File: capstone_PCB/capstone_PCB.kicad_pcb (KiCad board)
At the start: 2 copper layers, 110 x 65 mm, 48 parts, among them J1 282837-4, J2 282837-4, J3 Barrel Jack, J4 282837-4, J5 Fan1, J6 Fan2, J7 12402012E212A, P1 282837-2, P3 282837-2, P4 282837-2, P5 282837-2, Q1 IRF4905PBF, U1 DEV-15583, U2 2472, U3 VNH5019ATR-E, U4 VNH5019ATR-E

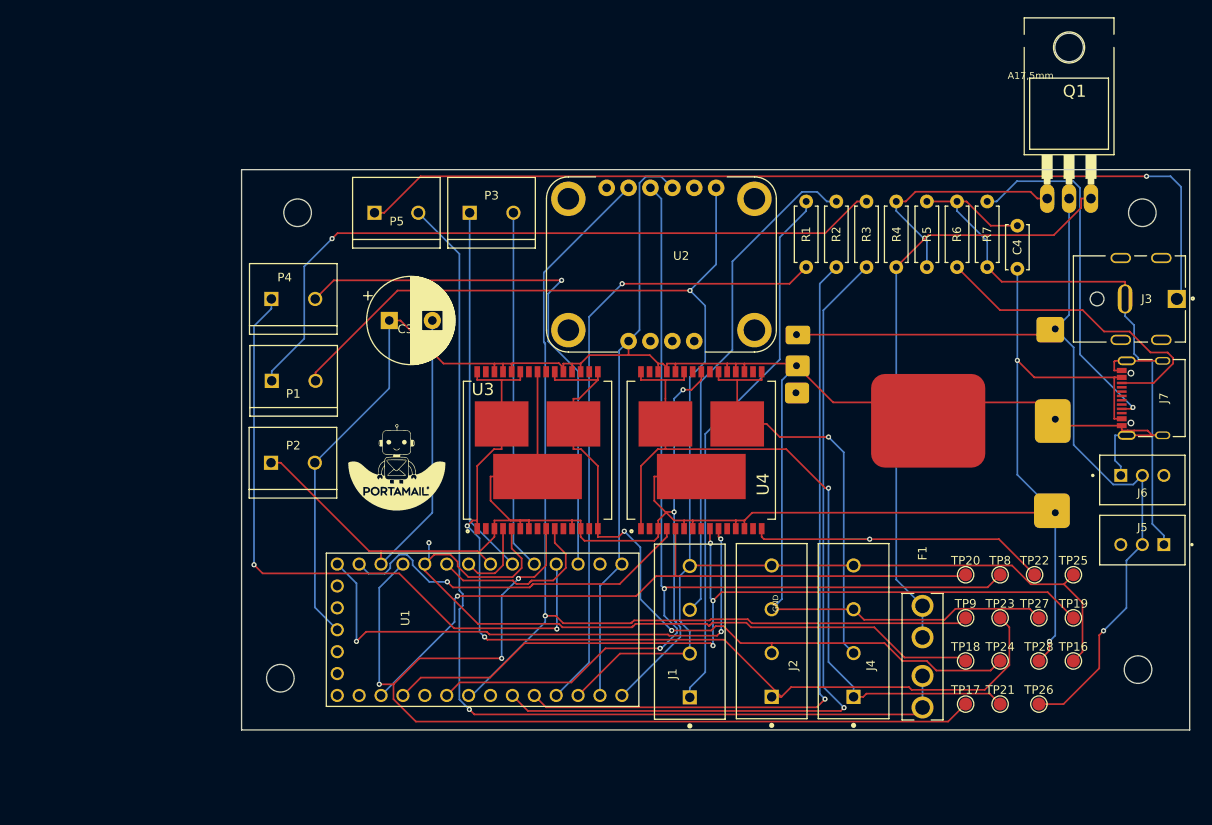
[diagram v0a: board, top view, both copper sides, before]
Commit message: Updated Capstone PCB to new iteration with esp32
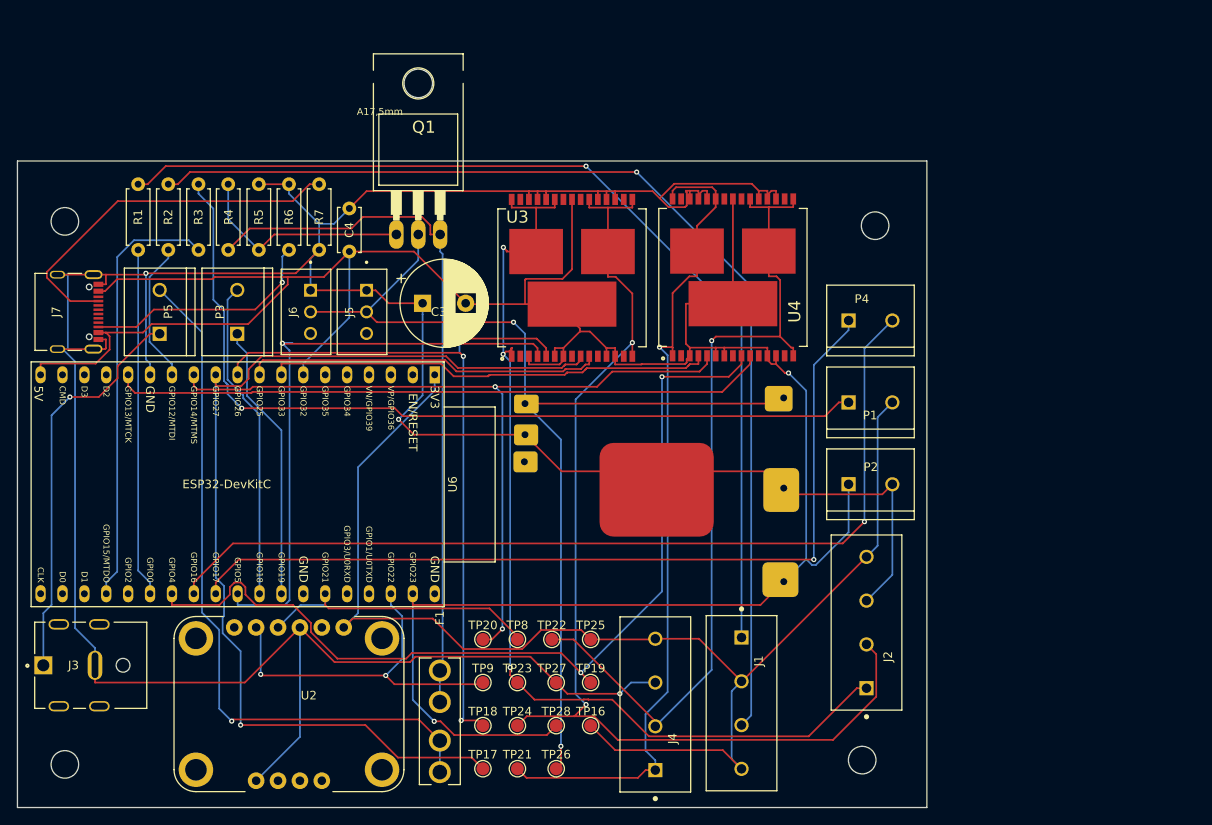
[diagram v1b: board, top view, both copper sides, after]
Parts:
- removed G***: LOGO, LOGO
- removed U1: DEV-15583, DEV-15583:MODULE_DEV-15583
- added U6: ESP32-DevKitC, PCM_Espressif:ESP32-DevKitC, F.Cu at (542.9, 10.3)
- moved J7 128.6 mm to (499.1, 3.00), turned to -90 degrees
- moved J3 127.8 mm to (503.0, 44.0), turned to 180 degrees
- moved J6 99.0 mm to (528.0, 3.00), turned to 90 degrees
- moved J5 94.3 mm to (534.5, 3.00), turned to 90 degrees
- moved C4 77.5 mm to (533.0, -4.00)
- moved R1 77.5 mm to (508.5, -4.19)
- moved R2 77.5 mm to (512.0, -4.19)
- moved R3 77.5 mm to (515.5, -4.19)
- moved R4 77.5 mm to (519.0, -4.19)
- moved R5 77.5 mm to (522.5, -4.19)
- moved R6 77.5 mm to (526.0, -4.19)
- moved R7 77.5 mm to (529.5, -4.19)
- moved Q1 75.6 mm to (541.0, -12.3)
- moved P2 67.0 mm to (593.5, 23.0)
- moved P4 67.0 mm to (593.5, 4.00)
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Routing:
- net Net-(U2-SDA): track 122.2 -> 33.3 mm, vias 2 -> 0
- net Net-(U2-SCL): track 117.1 -> 43.6 mm, vias 1 -> 2
- net Net-(U6-GPIO12): track 85.9 -> 16.5 mm, vias 1 -> 0
- net Net-(J1-Pad3): track 58.3 -> 125.1 mm, vias 0 -> 1
- net Net-(J3-Pad1): track 109.0 -> 46.7 mm
- net Net-(U3-INA): track 9.06 -> 70.9 mm, vias 0 -> 1
- net Net-(J1-Pad1): track 63.1 -> 115.0 mm, vias 0 -> 1
- net Net-(U6-GPIO15): track 93.6 -> 50.3 mm, vias 1 -> 0
- net Net-(U6-GPIO16): track 64.5 -> 106.7 mm
- net Net-(J2-Pad2): track 87.5 -> 124.8 mm
- net Net-(F1-Pad1_1): track 117.2 -> 82.4 mm
- net Net-(U6-GPIO0): track 73.1 -> 40.5 mm, vias 1 -> 0
- net VCC: track 290.5 -> 317.9 mm, vias 4 -> 2
- net GNDA: track 368.3 -> 393.8 mm, vias 0 -> 3
- net Net-(U6-GPIO17): track 77.5 -> 101.2 mm, vias 2 -> 1
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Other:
- board size 110 x 65 mm -> 105.5 x 75 mm
